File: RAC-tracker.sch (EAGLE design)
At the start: 5 parts

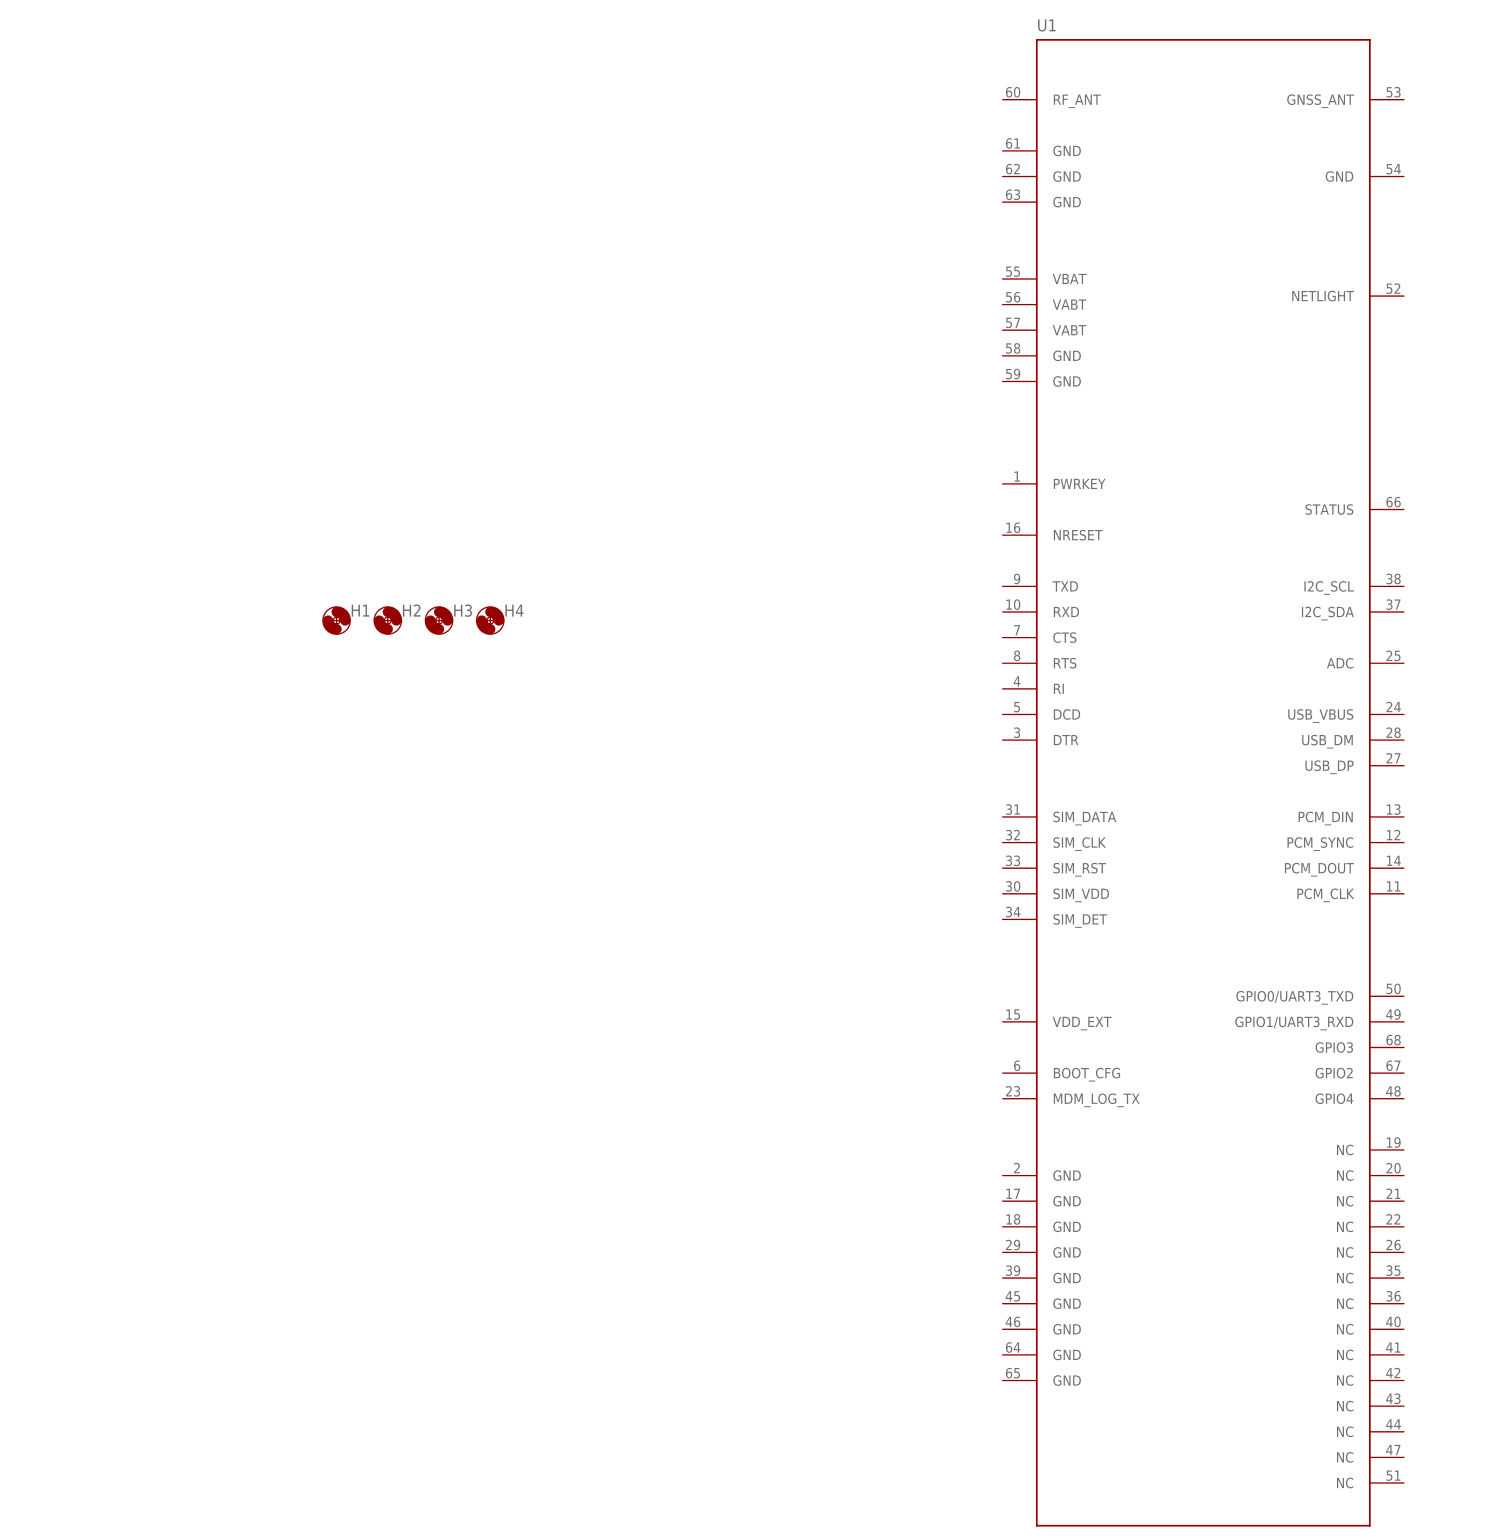
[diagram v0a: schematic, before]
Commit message: Started connecting the SIM7000
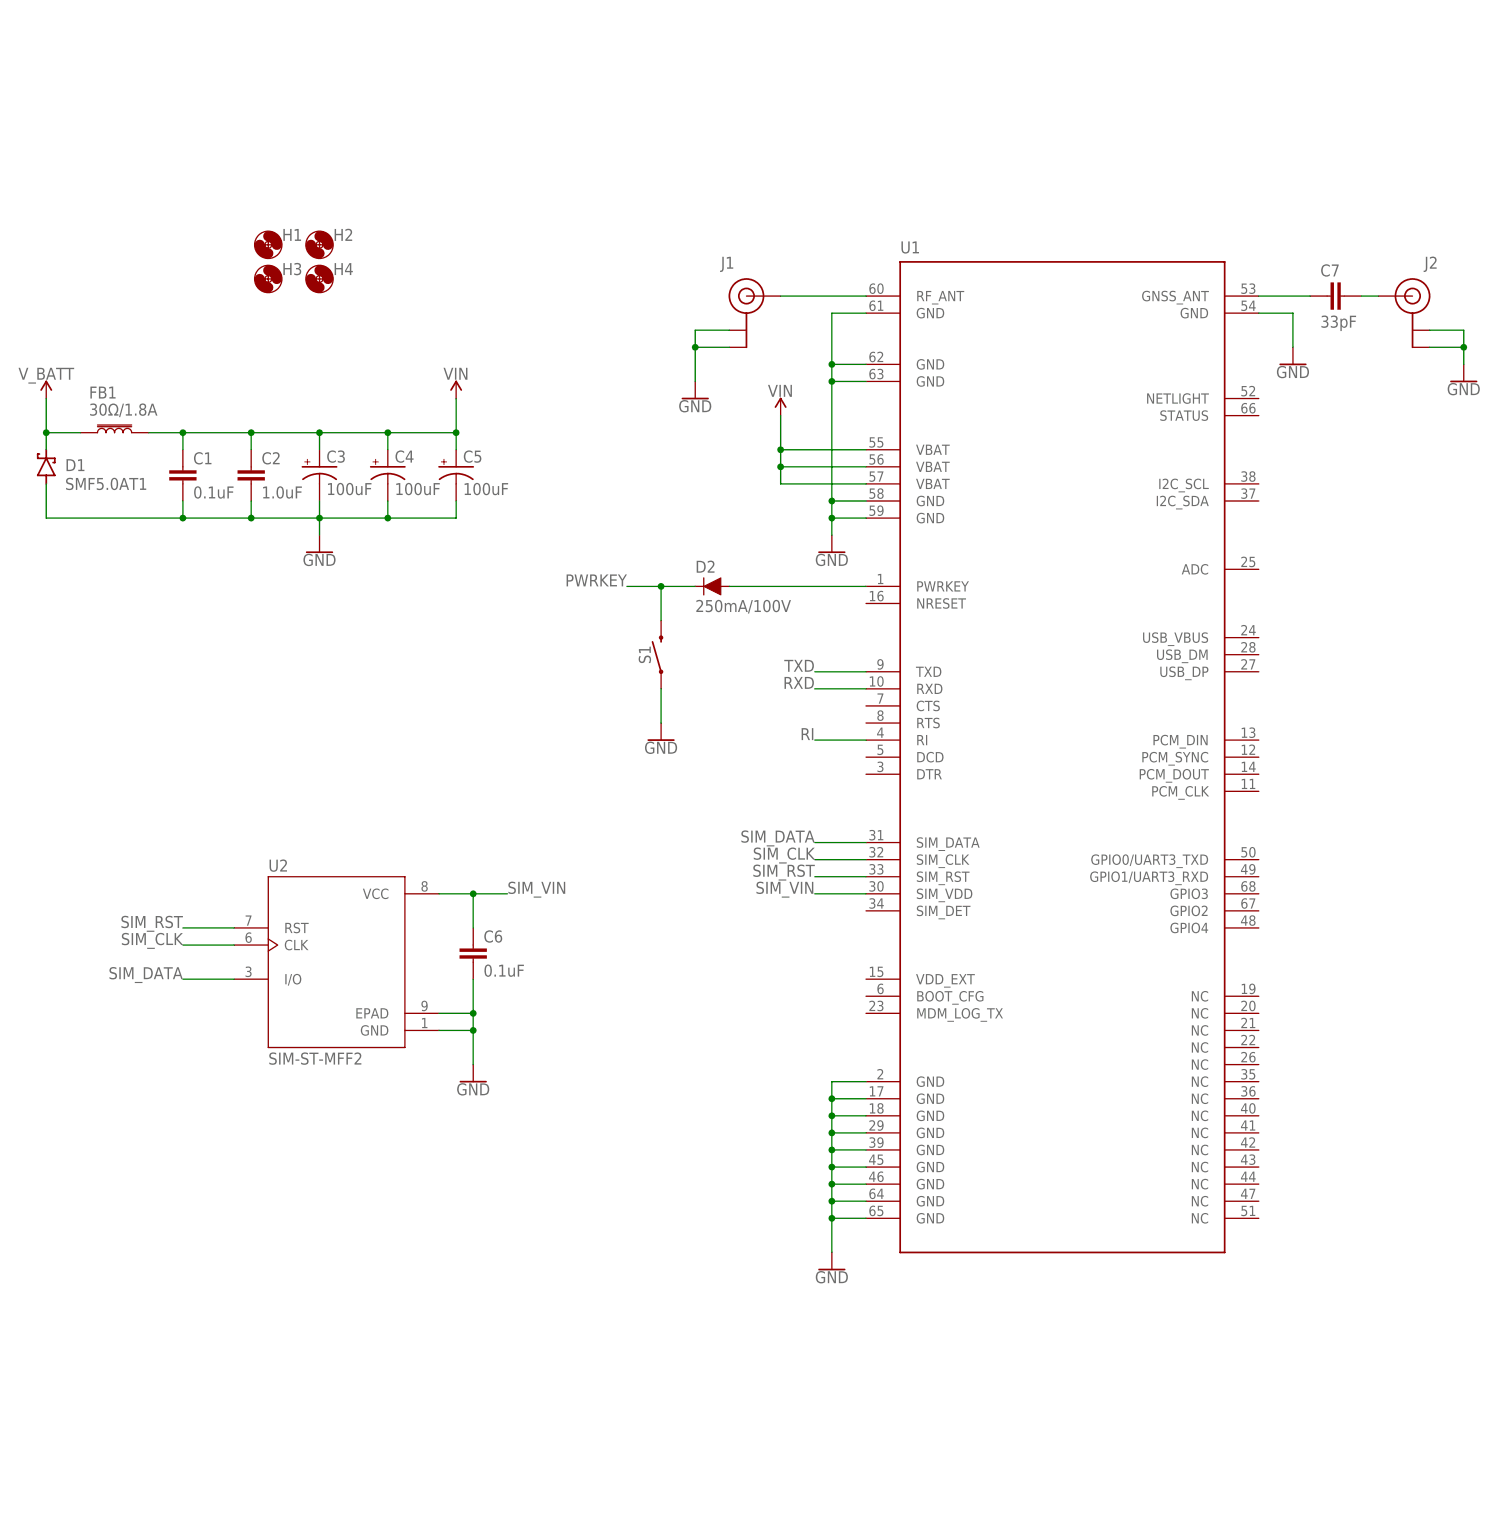
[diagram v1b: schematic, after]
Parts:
- added C1, C6: 0.1uF, SparkFun-Capacitors:0.1UF-0603-25V-(+80/-20%)
- added C2: 1.0uF, SparkFun-Capacitors:1.0UF-0603-16V-10%
- added C3, C4, C5: 100uF, SparkFun-Capacitors:100UF-POLAR-EIA7343-10V-10%(TANT)
- added C7: 33pF, SparkFun-Capacitors:33PF-0603-50V-5%
- added D1: SMF5.0AT1, diode:SMF5.0AT1
- added D2: 250mA/100V, SparkFun-DiscreteSemi:DIODE-BAS16J
- added FB1: 30Ω/1.8A, SparkFun-Coils:FERRITE_BEAD-0603
- added J1, J2: U.FL, SparkFun-Connectors:U.FL
- added S1: MOMENTARY-SWITCH-SPST-SMD-5.2MM, SparkFun-Switches:MOMENTARY-SWITCH-SPST-SMD-5.2MM
- added U2: SIM-ST-MFF2, rocket-components:SIM-ST-MFF2
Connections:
- new net GND: C1.2, C2.2, C3.-, C4.-, C5.-, C6.2, D1.A, J1.GND@0, J1.GND@1, J2.GND@0, J2.GND@1, S1.1, U1.GND, U1.GND@1, U1.GND@10, U1.GND@11, U1.GND@12, U1.GND@13, U1.GND@14, U1.GND@2, U1.GND@3, U1.GND@4, U1.GND@5, U1.GND@6, U1.GND@7, U1.GND@8, U1.GND@9, U2.EPAD, U2.GND
- new net N$1: J1.SIGNAL, U1.RF_ANT
- new net N$2: C7.1, U1.GNSS_ANT
- new net N$3: C7.2, J2.SIGNAL
- new net PWRKEY: D2.C, S1.2
- new net PWRKEY_AN: D2.A, U1.PWRKEY
- new net RI: U1.RI
- new net RXD: U1.RXD
- new net SIM_CLK: U1.SIM_CLK, U2.CLK
- new net SIM_DATA: U1.SIM_DATA, U2.I/O
- new net SIM_RST: U1.SIM_RST, U2.RST
- new net SIM_VIN: C6.1, U1.SIM_VDD, U2.VCC
- new net TXD: U1.TXD
- new net VIN: C1.1, C2.1, C3.+, C4.+, C5.+, FB1.2, U1.VBAT, U1.VBAT@1, U1.VBAT@2
- new net V_BATT: D1.C, FB1.1
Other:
- moved on the sheet: H1, H2, H3, H4, U1

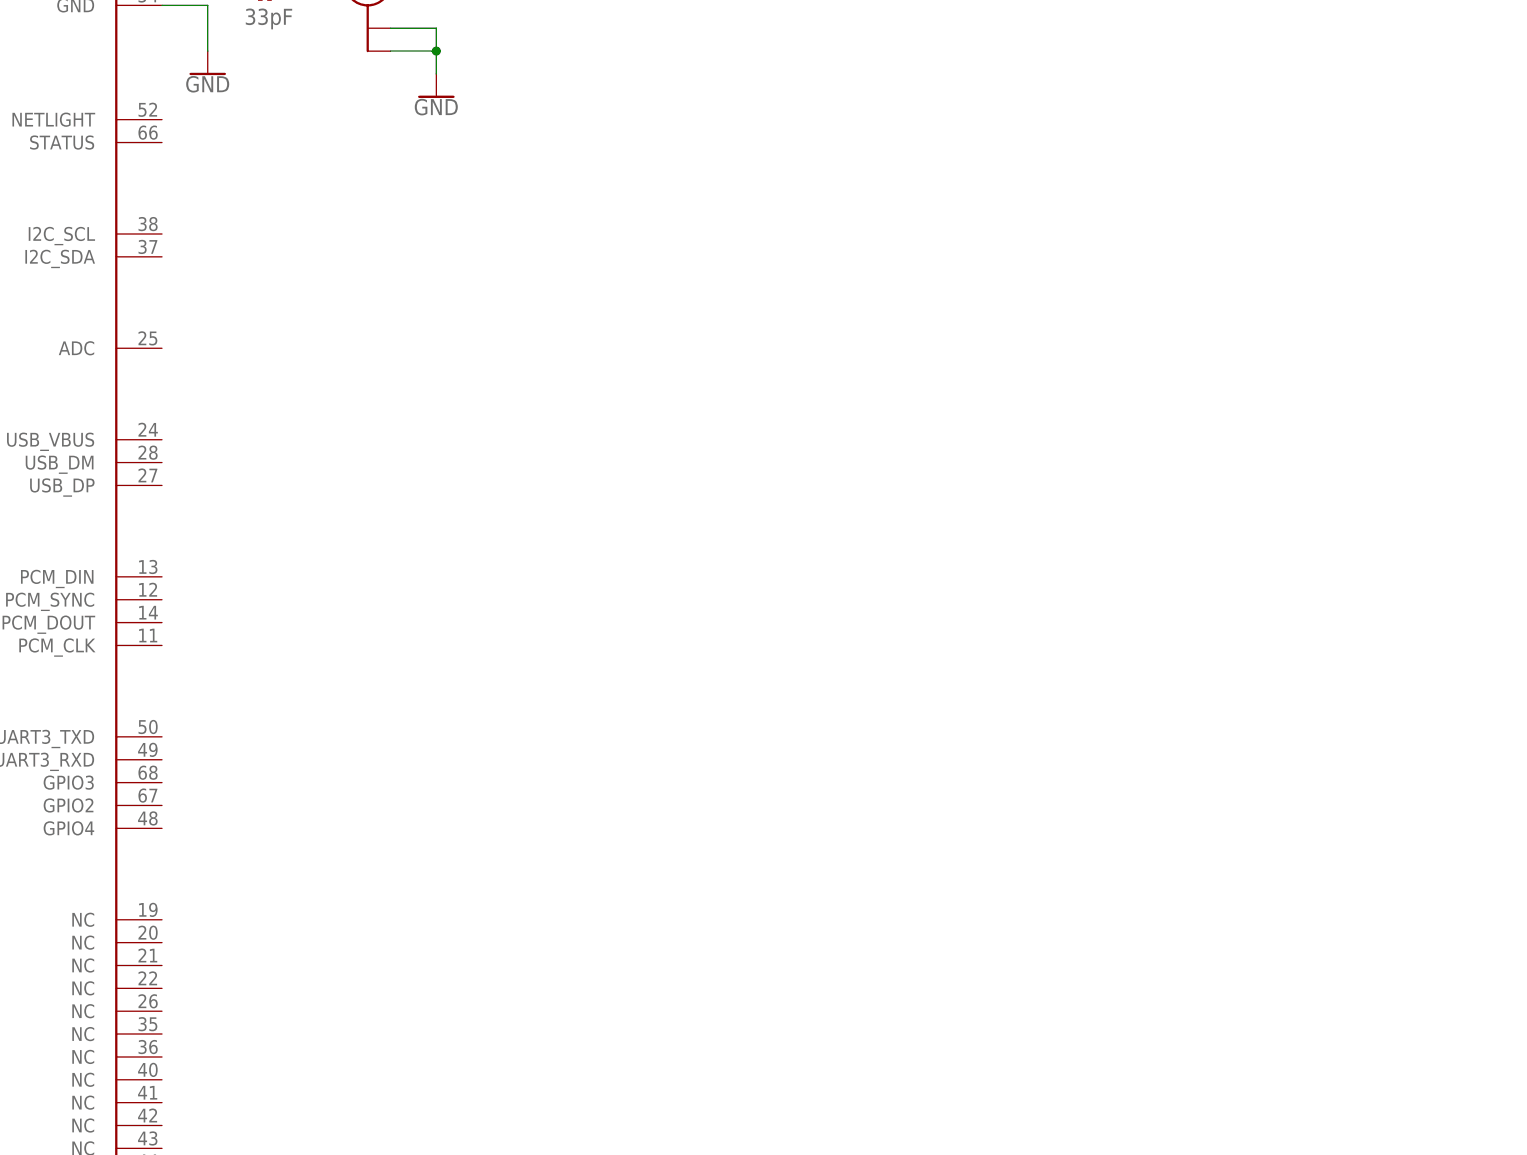
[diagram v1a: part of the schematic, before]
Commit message: Added LiPo charging circuit, LiPo connector, and USB connector
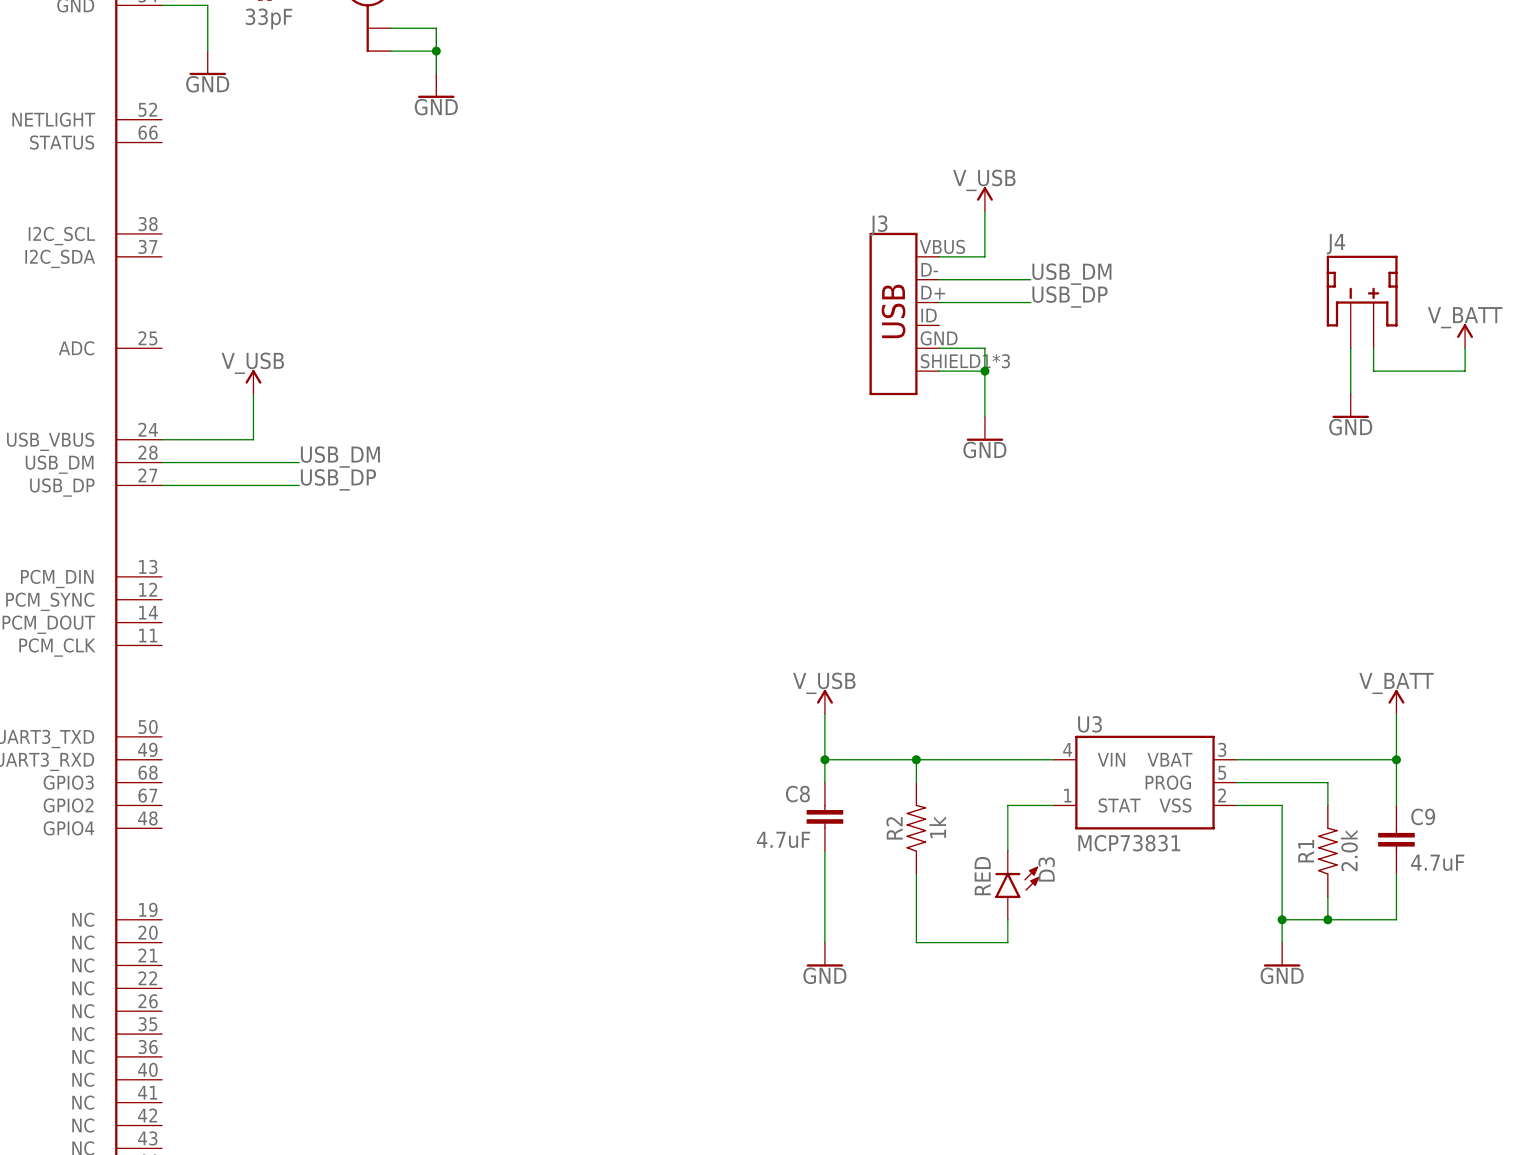
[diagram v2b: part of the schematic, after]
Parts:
- added C8, C9: 4.7uF, SparkFun-Capacitors:4.7UF0603
- added D3: RED, SparkFun-LED:LED-RED0603
- added J3: (no value), SparkFun-Connectors:USB_MICRO-B_FEMALE-SMT
- added J4: (no value), SparkFun-Connectors:JST_2MM_MALE
- added R1: 2.0k, SparkFun-Resistors:2.0KOHM-0603-1/10W-5%
- added R2: 1k, SparkFun-Resistors:1KOHM-0603-1/10W-1%
- added U3: MCP73831, SparkFun-IC-Power:MCP73831
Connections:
- new net N$4: R1.2, U3.PROG
- new net N$5: D3.C, U3.STAT
- new net N$6: D3.A, R2.1
- new net USB_DM: J3.D-, U1.USB_DM
- new net USB_DP: J3.D+, U1.USB_DP
- new net V_USB: C8.1, J3.VBUS, R2.2, U1.USB_VBUS, U3.VIN
- net GND: now also C8.2, C9.2, J3.GND, J3.SHIELD, J4.-, R1.1, U3.VSS
- net V_BATT: now also C9.1, J4.+, U3.VBAT

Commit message: Renamed nets and started board placement
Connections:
- net N$1 renamed LTE_OUT
- net N$2 renamed GNSS_RF
- net N$3 renamed GNSS_OUT
- net N$4 renamed PROG
- net N$5 renamed STAT
- net N$6 renamed STAT_AN
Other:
- moved on the sheet: C8, R2
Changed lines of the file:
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@@
 <attribute name="VALUE" x="208.28" y="-58.674" size="1.778" layer="96" align="top-center"/>
 </instance>
-<instance part="C8" gate="G$1" x="157.48" y="-43.18" smashed="yes" rot="MR0">
-<attribute name="NAME" x="155.956" y="-40.259" size="1.778" layer="95" font="vector" rot="MR0"/>
-<attribute name="VALUE" x="155.956" y="-45.339" size="1.778" layer="96" font="vector" rot="MR0"/>
+<instance part="C8" gate="G$1" x="157.48" y="-45.72" smashed="yes" rot="MR0">
+<attribute name="NAME" x="155.956" y="-42.799" size="1.778" layer="95" font="vector" rot="MR0"/>
+<attribute name="VALUE" x="155.956" y="-47.879" size="1.778" layer="96" font="vector" rot="MR0"/>
 </instance>
 <instance part="C9" gate="G$1" x="220.98" y="-45.72" smashed="yes">
@@
 <attribute name="VALUE" x="175.895" y="-46.228" size="1.778" layer="96" font="vector" rot="R270" align="top-left"/>
 </instance>
-<instance part="R2" gate="G$1" x="167.64" y="-43.18" smashed="yes" rot="R90">
-<attribute name="NAME" x="166.116" y="-43.18" size="1.778" layer="95" font="vector" rot="R90" align="bottom-center"/>
-<attribute name="VALUE" x="169.164" y="-43.18" size="1.778" layer="96" font="vector" rot="R90" align="top-center"/>
+<instance part="R2" gate="G$1" x="167.64" y="-45.72" smashed="yes" rot="R90">
+<attribute name="NAME" x="166.116" y="-45.72" size="1.778" layer="95" font="vector" rot="R90" align="bottom-center"/>
+<attribute name="VALUE" x="169.164" y="-45.72" size="1.778" layer="96" font="vector" rot="R90" align="top-center"/>
 </instance>
 <instance part="GND11" gate="1" x="157.48" y="-58.42" smashed="yes">
@@
 <pinref part="C8" gate="G$1" pin="2"/>
 <pinref part="GND11" gate="1" pin="GND"/>
-<wire x1="157.48" y1="-45.72" x2="157.48" y2="-55.88" width="0.1524" layer="91"/>
+<wire x1="157.48" y1="-48.26" x2="157.48" y2="-55.88" width="0.1524" layer="91"/>
 </segment>
 <segment>
@@
 </segment>
 </net>
-<net name="N$1" class="0">
+<net name="LTE_OUT" class="0">
 <segment>
 <pinref part="U1" gate="G$1" pin="RF_ANT"/>
@@
 </segment>
 </net>
-<net name="N$2" class="0">
+<net name="GNSS_RF" class="0">
 <segment>
 <pinref part="U1" gate="G$1" pin="GNSS_ANT"/>
@@
 </segment>
 </net>
-<net name="N$3" class="0">
+<net name="GNSS_OUT" class="0">
 <segment>
 <pinref part="C7" gate="G$1" pin="2"/>
@@
 <segment>
 <pinref part="R2" gate="G$1" pin="2"/>
-<wire x1="167.64" y1="-38.1" x2="167.64" y2="-35.56" width="0.1524" layer="91"/>
+<wire x1="167.64" y1="-40.64" x2="167.64" y2="-35.56" width="0.1524" layer="91"/>
 <pinref part="U3" gate="G$1" pin="VIN"/>
 <wire x1="167.64" y1="-35.56" x2="182.88" y2="-35.56" width="0.1524" layer="91"/>
@@
 <junction x="167.64" y="-35.56"/>
 <pinref part="C8" gate="G$1" pin="1"/>
-<wire x1="157.48" y1="-35.56" x2="157.48" y2="-38.1" width="0.1524" layer="91"/>
+<wire x1="157.48" y1="-35.56" x2="157.48" y2="-40.64" width="0.1524" layer="91"/>
 <pinref part="SUPPLY6" gate="G$1" pin="V_USB"/>
 <wire x1="157.48" y1="-30.48" x2="157.48" y2="-35.56" width="0.1524" layer="91"/>
@@
 </segment>
 </net>
-<net name="N$4" class="0">
+<net name="PROG" class="0">
 <segment>
 <pinref part="U3" gate="G$1" pin="PROG"/>
@@
 </segment>
 </net>
-<net name="N$5" class="0">
+<net name="STAT" class="0">
 <segment>
 <pinref part="D3" gate="G$1" pin="C"/>
@@
 </segment>
 </net>
-<net name="N$6" class="0">
+<net name="STAT_AN" class="0">
 <segment>
 <pinref part="D3" gate="G$1" pin="A"/>
@@
 <wire x1="177.8" y1="-55.88" x2="167.64" y2="-55.88" width="0.1524" layer="91"/>
 <pinref part="R2" gate="G$1" pin="1"/>
-<wire x1="167.64" y1="-55.88" x2="167.64" y2="-48.26" width="0.1524" layer="91"/>
-</segment>
-</net>
+<wire x1="167.64" y1="-55.88" x2="167.64" y2="-50.8" width="0.1524" layer="91"/>
+</segment>
+</net>
